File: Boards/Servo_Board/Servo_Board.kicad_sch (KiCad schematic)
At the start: 73 parts, among them J1 DB9 Microfit, J10 I2CA JST, J11 I2CB JST, J12 I2CC JST, J13 SERVO A, J14 SERVO B, J15 SERVO C, J16 SERVO D, J2 DB9 Microfit, J3 CAN1_T, J4 CAN1_T, J5 USB_B_Micro, J6 SWD JST PH, J7 UART JST, J8 AUX BATT CONN, J9 Extras JST, Q1 DMP6023LFG, U1 AZ1117C-5.0, U2 STM32G0B1RCTx, U3 TCAN1046, U4 AZ1117C-3.3, Y1 8MHz

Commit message: Somewhat done servo+adc boards
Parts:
- removed C1: 100u, Capacitor_SMD:CP_Elec_8x10.5, symbol Device:C_Polarized
- removed C2, C4: 10u, Capacitor_SMD:C_0603_1608Metric, symbol Device:C
- removed C3, C5: 22u, Capacitor_SMD:C_1206_3216Metric, symbol Device:C
- removed J1, J2: DB9 Microfit, Connector_Molex:Molex_Micro-Fit_3.0_43045-1012_2x05_P3.00mm_Vertical, symbol Connector:DE9_Socket
- removed J10: I2CA JST, Connector_JST:JST_PH_B5B-PH-K_1x05_P2.00mm_Vertical, symbol Connector_Generic:Conn_01x05
- removed J12: I2CC JST, Connector_JST:JST_PH_B5B-PH-K_1x05_P2.00mm_Vertical, symbol Connector_Generic:Conn_01x05
- removed J3, J4: CAN1_T, Connector_PinHeader_2.54mm:PinHeader_1x02_P2.54mm_Vertical, symbol Connector_Generic:Conn_01x02
- removed J5: USB_B_Micro, Connector_USB:USB_Micro-B_Amphenol_10118193-0001LF_Horizontal, symbol Connector:USB_B_Micro
- removed J6: SWD JST PH, Connector_JST:JST_PH_B4B-PH-K_1x04_P2.00mm_Vertical, symbol Connector_Generic:Conn_01x04
- removed J7: UART JST, Connector_JST:JST_PH_B3B-PH-K_1x03_P2.00mm_Vertical, symbol Connector_Generic:Conn_01x03
- removed J9: Extras JST, Connector_JST:JST_PH_B7B-PH-K_1x07_P2.00mm_Vertical, symbol Connector_Generic:Conn_01x07
- removed R11: 9K53, Resistor_SMD:R_0603_1608Metric, symbol Device:R
- removed TP14: RS422TX, TestPoint:TestPoint_Pad_1.5x1.5mm, symbol Connector:TestPoint_Small
- removed TP16: RS422RX, TestPoint:TestPoint_Pad_1.5x1.5mm, symbol Connector:TestPoint_Small
- removed TP2: ADC4S, TestPoint:TestPoint_Pad_1.5x1.5mm, symbol Connector:TestPoint_Small
- removed TP3: ADC2S, TestPoint:TestPoint_Pad_1.5x1.5mm, symbol Connector:TestPoint_Small
- removed TP31: ADC2, TestPoint:TestPoint_Pad_1.5x1.5mm, symbol Connector:TestPoint_Small
- removed TP32: ADC3, TestPoint:TestPoint_Pad_1.5x1.5mm, symbol Connector:TestPoint_Small
- removed TP4: SPISCK, TestPoint:TestPoint_Pad_1.5x1.5mm, symbol Connector:TestPoint_Small
- removed TP5: SPIMISO, TestPoint:TestPoint_Pad_1.5x1.5mm, symbol Connector:TestPoint_Small
- removed TP7: SPICS, TestPoint:TestPoint_Pad_1.5x1.5mm, symbol Connector:TestPoint_Small
- removed U1: AZ1117C-5.0, Package_TO_SOT_SMD:SOT-223-3_TabPin2, symbol Regulator_Linear:AZ1117-5.0
- added C10, C16, C19, C20: 100n, Capacitor_SMD:C_0603_1608Metric, symbol Device:C
- added C11, C13: 22u, Capacitor_SMD:C_1206_3216Metric, symbol Device:C
- added C12, C14: 10u, Capacitor_SMD:C_0603_1608Metric, symbol Device:C
- added C15, C17, C21, C22: 100u, Capacitor_SMD:CP_Elec_6.3x5.9, symbol Device:C_Polarized
- added C18: 100u, Capacitor_SMD:CP_Elec_8x10.5, symbol Device:C_Polarized
- added C23: 100n, symbol Device:C
- added D1: LED_R, LED_SMD:LED_1206_3216Metric, symbol Device:LED
- added D10: 9V 15.4VC, Diode_SMD:D_SOD-123F, symbol Device:D_TVS
- added D2: LED_G, LED_SMD:LED_1206_3216Metric, symbol Device:LED
- added D3: LED_B, LED_SMD:LED_1206_3216Metric, symbol Device:LED
- added D8: D_0.5VF, Diode_SMD:D_SOD-523, symbol Device:D_Schottky
- added D9: 2.5V Ref Zener, Package_TO_SOT_SMD:SOT-23-3, symbol Device:D_Zener
- added J1: SWD JST PH, Connector_JST:JST_PH_B4B-PH-K_1x04_P2.00mm_Vertical, symbol Connector_Generic:Conn_01x04
- added J10, J9: CAN1_T, Connector_PinHeader_2.54mm:PinHeader_1x02_P2.54mm_Vertical, symbol Connector_Generic:Conn_01x02
- added J12, J6: DB9 Microfit, Connector_Molex:Molex_Micro-Fit_3.0_43045-1012_2x05_P3.00mm_Vertical, symbol Connector:DE9_Socket
- added J2: UART JST, Connector_JST:JST_PH_B3B-PH-K_1x03_P2.00mm_Vertical, symbol Connector_Generic:Conn_01x03
- added J3: Extras JST, Connector_JST:JST_PH_B7B-PH-K_1x07_P2.00mm_Vertical, symbol Connector_Generic:Conn_01x07
- added J4: USB_B_Micro, Connector_USB:USB_Micro-B_Amphenol_10118193-0001LF_Horizontal, symbol Connector:USB_B_Micro
- added J5: I2CA JST, Connector_JST:JST_PH_B5B-PH-K_1x05_P2.00mm_Vertical, symbol Connector_Generic:Conn_01x05
- added J7: I2CB JST, Connector_JST:JST_PH_B5B-PH-K_1x05_P2.00mm_Vertical, symbol Connector_Generic:Conn_01x05
- added J8: SPI JST, Connector_JST:JST_PH_B6B-PH-K_1x06_P2.00mm_Vertical, symbol Connector_Generic:Conn_01x06
- added R10: 100K, Resistor_SMD:R_0603_1608Metric, symbol Device:R
- added R15, R16, R20, R21: 100k, Resistor_SMD:R_0603_1608Metric, symbol Device:R
- added R19: 9K53, Resistor_SMD:R_0603_1608Metric, symbol Device:R
- added R22: 22K, symbol Device:R
- added R23: 15K, symbol Device:R
- added R24: 6K2, symbol Device:R
- added R25: 4K7, symbol Device:R
- added R26: 1K5, symbol Device:R
- added R6: 0R, Resistor_SMD:R_0603_1608Metric, symbol Device:R
- added R9: 120R, Resistor_SMD:R_0603_1608Metric, symbol Device:R
- added U4: AZ1117C-5.0, Package_TO_SOT_SMD:SOT-223-3_TabPin2, symbol Regulator_Linear:AZ1117-5.0
- added U5: TPS2121RUXR, Custom:RUX0012A, symbol TS_Symbols:TPS2121RUXR
- F1: value 2A -> 5A; footprint (none) -> Fuse:Fuse_1206_3216Metric
- F2: value 2A -> 5A; footprint (none) -> Fuse:Fuse_1206_3216Metric; now fitted
- J11: value I2CB JST -> I2CC JST
- JP1, JP2: footprint (none) -> Jumper:SolderJumper-3_P1.3mm_Bridged12_RoundedPad1.0x1.5mm
- R1: value 100K -> 549R; footprint (none) -> Resistor_SMD:R_0603_1608Metric
- R11: renamed from R8; footprint (none) -> Resistor_SMD:R_0603_1608Metric
- R12: value 0R -> 100K
- R13, R14: value 0R -> 100K; now fitted; now in the parts list
- R2, R3: value 100K -> 220R; footprint (none) -> Resistor_SMD:R_0603_1608Metric
- R4: value 100K -> 0R; footprint (none) -> Resistor_SMD:R_0603_1608Metric
- R5: value 120R -> 0R; footprint (none) -> Resistor_SMD:R_0603_1608Metric; now not fitted; now left out of the parts list
- renumbered C8 to C1, C6 to C2, C7 to C3, C10 to C4, C9 to C5, C11 to C6, C12 to C7, C14 to C8, C13 to C9, D3 to D5, D2 to D6, D1 to D7, J8 to J13, J13 to J15, J15 to J16, J16 to J17, R10 to R17, R9 to R18, R6 to R7, R7 to R8, TP9 to TP1, TP8 to TP2, U2 to U1, U3 to U2, U4 to U3
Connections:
- net 2S_VOLTAGE is gone; now on net 2S+ A10: R17.2
- net USART1_RX is gone; now on net CAN2_AUX: U1.61 (PB7)
- net +3V3: now also R13.1, R14.2, R4.1, C11.1, J5.5 (Pin_5), J7.5 (Pin_5), J8.6 (Pin_6), R10.2, R23.1, R26.1; no longer R1.1, R2.1, R3.2, R4.2
- net +5V: now also R5.1, C12.1, C13.1, J5.3 (Pin_3), J7.3 (Pin_3), U4.2 (VO); no longer R13.1
- net +7V4: now also R1.1, C15.1, C17.1, C21.1, C22.1, R6.1; no longer D6.1 (K), Q1.1 (S), Q1.2 (S), Q1.3 (S), R14.1, R17.1
- net +7V4_CAN: now also J12.1, J12.5, J6.1, J6.5
- net CAN1_AUX: now also U1.64 (PC10), J6.3; no longer U1.33 (PB13)
- net CAN1_RX: now also U1.62 (PB8); no longer U1.27 (PB0)
- net CAN1_TX: now also U1.63 (PB9); no longer U1.28 (PB1)
- net CAN2_AUX: now also J12.3; no longer U1.32 (PB12)
- net CANH1: now also J12.6, J6.6, J9.1 (Pin_1)
- net CANH2: now also J12.8, J6.8, R9.2; no longer R5.2
- net CANL1: now also J10.1 (Pin_1), J12.7, J6.7
- net CANL2: now also J12.9, J6.9
- net E1: now also J3.2 (Pin_2)
- net E2: now also J3.3 (Pin_3)
- net E3: now also J3.5 (Pin_5)
- net E4: now also J3.6 (Pin_6)
- net GND: now also C10.2, C11.2, C12.2, C13.2, C14.2, C15.2, C16.2, C17.2, C18.2, C19.2, C20.2, C21.2, C22.2, D1.1 (K), D10.1 (A1), D2.1 (K), D3.1 (K), D8.1 (K), J1.2 (Pin_2), J12.2, J12.4, J2.2 (Pin_2), J3.1 (Pin_1), J3.7 (Pin_7), J4.5 (GND), J5.1 (Pin_1), J6.2, J6.4, J7.1 (Pin_1), J8.1 (Pin_1), R19.2, U4.1 (GND)
- net I2C1_SCL: now also U1.37 (PA9/UCPD1_DBCC1), J5.4 (Pin_4); no longer U1.62 (PB8)
- net I2C1_SDA: now also U1.42 (PA10/UCPD1_DBCC2), J5.2 (Pin_2); no longer U1.63 (PB9)
- net I2C2_SCL: now also J7.4 (Pin_4); no longer J11.4 (Pin_4)
- net I2C2_SDA: now also J7.2 (Pin_2); no longer J11.2 (Pin_2)
- net I2C3_SCL: now also J11.4 (Pin_4)
- net I2C3_SDA: now also J11.2 (Pin_2)
- net LED1: now also R2.1
- net NRST: now also J1.4 (Pin_4)
- net PWM_A: now also U1.38 (PC6)
- net PWM_B: now also U1.39 (PC7)
- net PWM_C: now also U1.36 (PA8)
- net PWM_D: now also U1.34 (PB14)
- net SPI_MISO: now also J8.2 (Pin_2)
- net SPI_MOSI: now also U1.24 (PA7), J8.4 (Pin_4)
- net SPI_SCK: now also J8.3 (Pin_3)
- net SWCLK: now also J1.1 (Pin_1)
- net SWDIO: now also J1.3 (Pin_3)
- net UART2_RX: now also D4.4 (K3), J2.1 (Pin_1)
- net UART2_TX: now also D4.5 (K4), J2.3 (Pin_3)
- net USB_D+: now also J4.3 (D+)
- net USB_D-: now also J4.2 (D-)
- net at D7.2 (A2), F1.1, Q1.5 (D): no longer F2.2
- net at R2.2: now also D2.2 (A); no longer U2.7 (RXD2)
- net at U2.14 (STB1): now also R10.1; no longer R4.1
- net at U2.6 (TXD2): now also R12.2; no longer R1.2
- net at U2.8 (STB2): now also R14.1; no longer R3.1
- net at J13.1 (Pin_1), J13.2 (Pin_2): now also F2.2; no longer F2.1
- net PWR_SOURCE: now reaches U1.1 (PC11)
- net PWR_SOURCE: now also R23.2, U5.9 (ST)
- net SYNC: now reaches U1.25 (PC4)
- net ~{ADC_RDY}: now reaches U1.26 (PC5)
- net 2S+ A10: now reaches U1.29 (PB2)
- net 2S+ A10: now also R19.1
- net A11: now reaches U1.30 (PB10)
- net ??PWM_AUX??: now reaches U1.35 (PB15)
- net LED2: now reaches U1.49 (PC9)
- net LED2: now also R3.1
- net at R11.1: now also J10.2 (Pin_2)
- net ADC_0 (4S) renamed POT_A A0
- net POT_A A0: now also C16.1, R16.2
- net ADC_1 (2S) renamed POT_B A1
- net POT_B A1: now also C10.1, R15.2
- net ADC_2 renamed POT_C A2
- net POT_C A2: now also C19.1, R20.2
- net ADC_3 renamed POT_D A3
- net POT_D A3: now also C20.1, R21.2
- net POT_A: no longer names the net of J15.4 (Pin_4)
- net POT_A: now also R16.1
- net POT_B: no longer names the net of J14.4 (Pin_4)
- net POT_B: now also R15.1
- net POT_C: no longer names the net of J16.4 (Pin_4)
- net POT_C: now also R20.1
- net POT_D: no longer names the net of J17.4 (Pin_4)
- net POT_D: now also R21.1
- net SPI_SD_CS renamed SPI_CS
- net SPI_CS: now also J8.5 (Pin_5)
- net USART1_TX: no longer names the net of U1.60 (PB6)
- new net: D3.2 (A), R3.2
- new net: R24.2, R25.1, U5.6 (PR1)
- new net: C23.2, D8.2 (A), D9.2 (A), R22.2, R25.2, U5.12 (GND), U5.4 (OV2), U5.5 (OV1)
- new net: D6.1 (K), Q1.1 (S), Q1.2 (S), Q1.3 (S), R24.1, U5.7 (IN1)
- new net: C14.1, C18.1, R17.1, U4.3 (VI), U5.1 (OUT), U5.8 (OUT)
- new net: D10.2 (A2), F2.1, U5.2 (IN2)
- new net: J3.4 (Pin_4), R4.2, R5.2, R6.2
- new net: R13.2, U2.7 (RXD2)
- new net: D9.1 (K), R26.2, U5.3 (CP2)
- new net: C23.1, U5.11 (SS)
- new net: R22.1, U5.10 (ILM)
- new net: D1.2 (A), R1.2
- new net: J9.2 (Pin_2), R9.1
- new net A9: U1.28 (PB1)
- new net ~{ADC_RST}: U1.27 (PB0)
- no-connect marks 17 -> 20
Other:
- note added: "1.2V dropout voltage makes V_{cr}=6.2V"
- note added: "100n gives slew limit of ~790V/s"
- note added: "Max peak: 55A Max continuous: ~6A"
- note added: "Provides RPP to stop current flowing back through TPS2121"
- note added: "RC cutoff frequency 15.9Hz"
- note added: "SPI"
- note added: "Setting to 22K gives 4.55A ILIM. ILIM=65.2/(RLIM^0.861)"
- note added: "Will switch to IN2 if PR1 drops below CP2. Want to switch at 6.3V."
- company: (none) -> Hybrid Test Stand
- title: (none) -> Servo ECU Board
- moved on the sheet: C1, C2, C3, C4, C5, C6, C7, C8, C9, D4A, D4B, D4C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

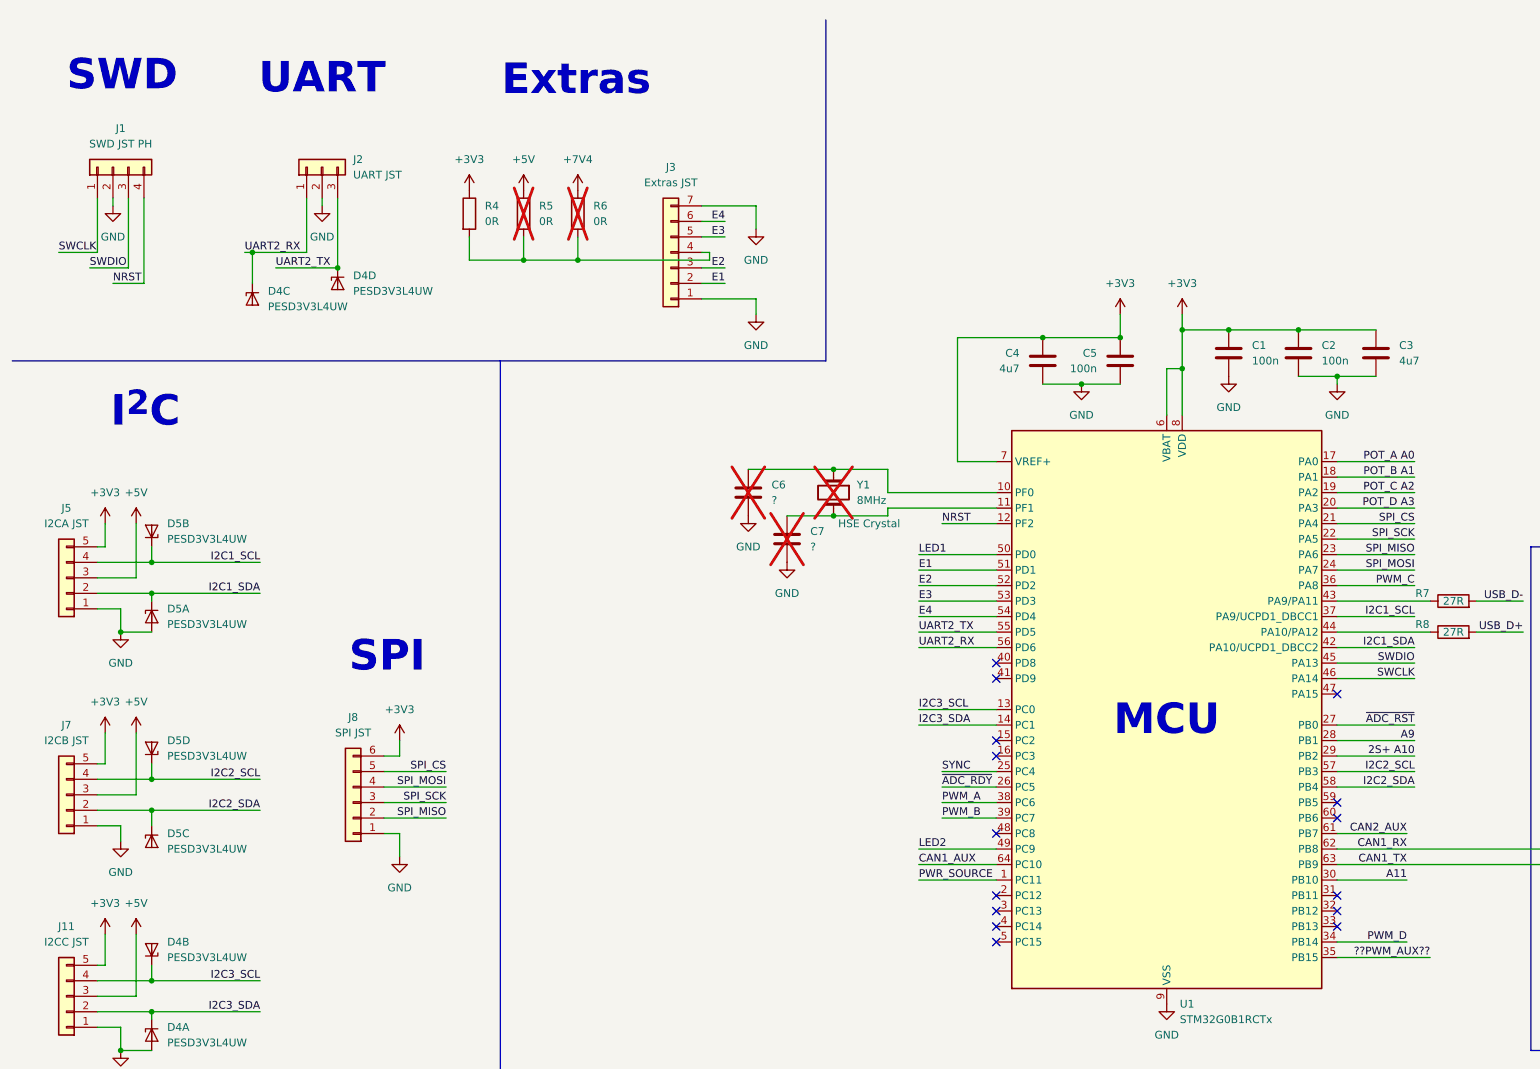
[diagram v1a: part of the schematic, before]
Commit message: Fixes and footprints
Just thermocouples todo
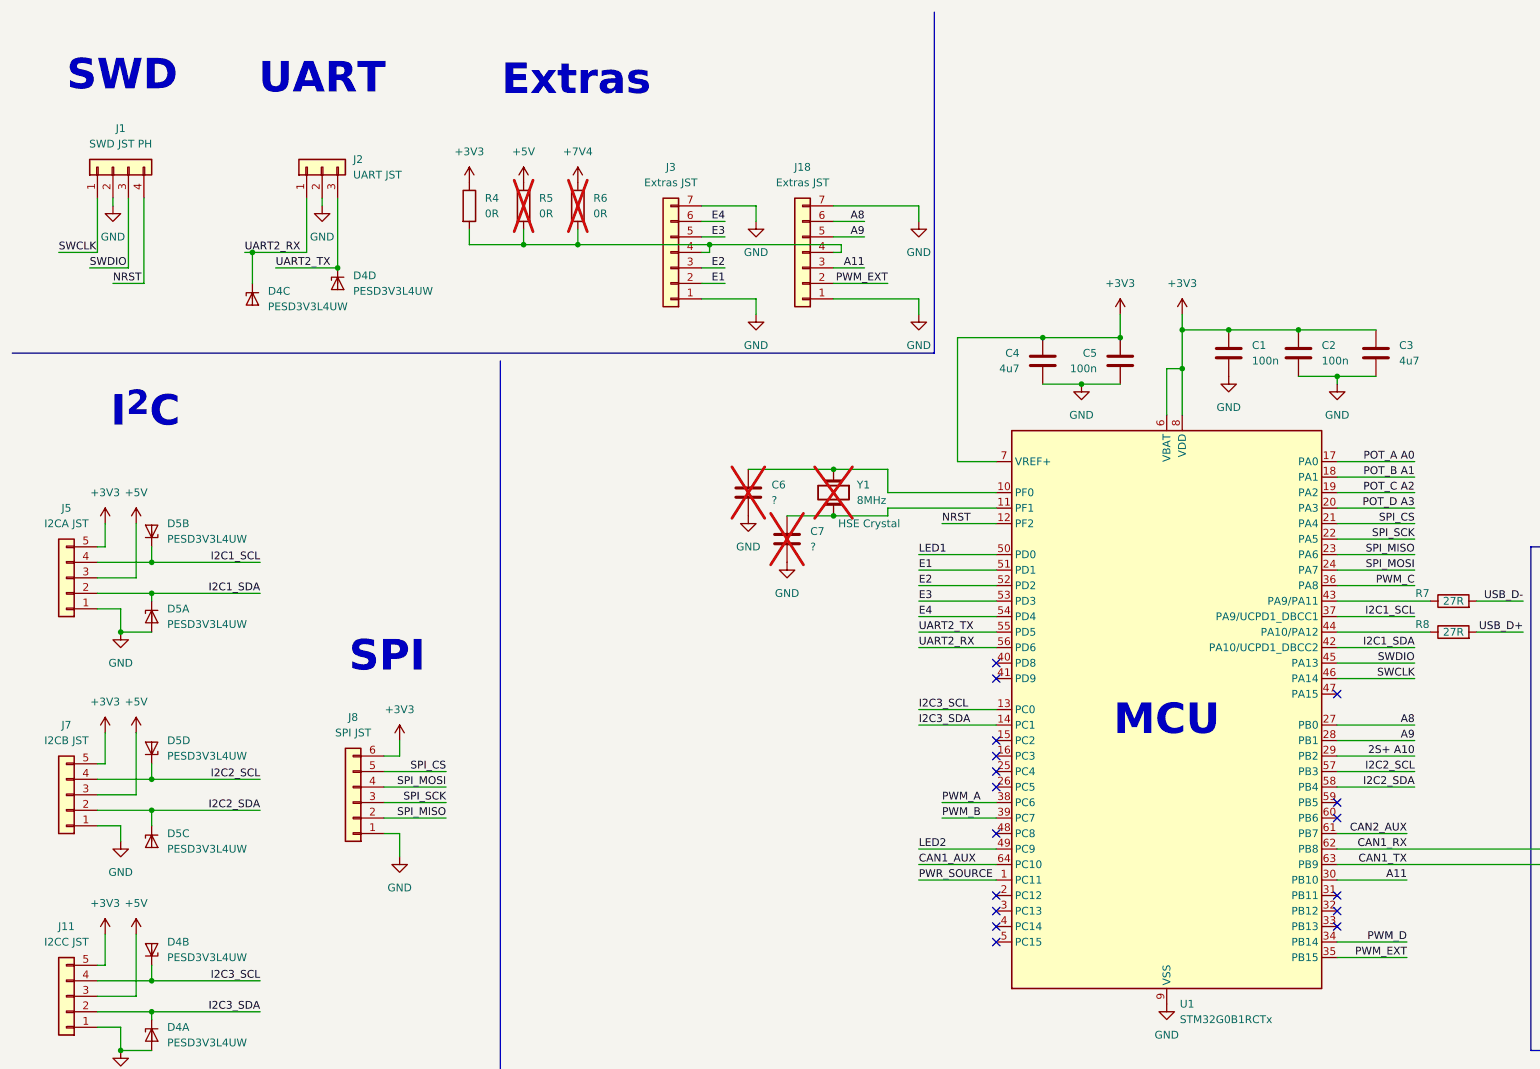
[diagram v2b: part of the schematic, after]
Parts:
- added J18: Extras JST, Connector_JST:JST_PH_B7B-PH-K_1x07_P2.00mm_Vertical, symbol Connector_Generic:Conn_01x07
- C23: footprint (none) -> Capacitor_SMD:C_0603_1608Metric
- R22, R23, R24, R25, R26: footprint (none) -> Resistor_SMD:R_0603_1608Metric
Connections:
- net A11: now also J18.3 (Pin_3)
- net A9: now also J18.5 (Pin_5)
- net GND: now also J18.1 (Pin_1), J18.7 (Pin_7)
- net at J3.4 (Pin_4), R4.2, R5.2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: now also J18.4 (Pin_4)
- net ??PWM_AUX?? renamed PWM_EXT
- net PWM_EXT: now also J18.2 (Pin_2)
- net SYNC: no longer names the net of U1.25 (PC4)
- net ~{ADC_RDY}: no longer names the net of U1.26 (PC5)
- net ~{ADC_RST} renamed A8
- net A8: now also J18.6 (Pin_6)
- no-connect marks 20 -> 22
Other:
- moved on the sheet: R4, R5, R6

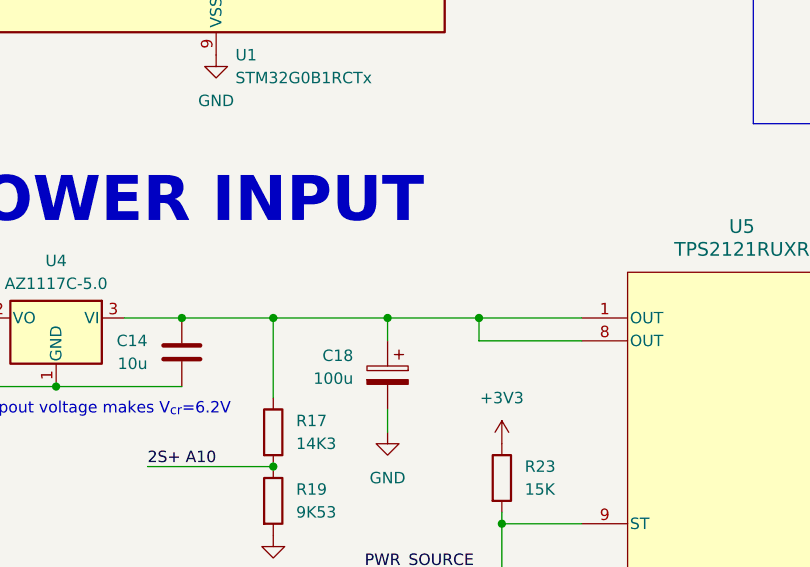
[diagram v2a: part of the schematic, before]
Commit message: Added switch to servo board
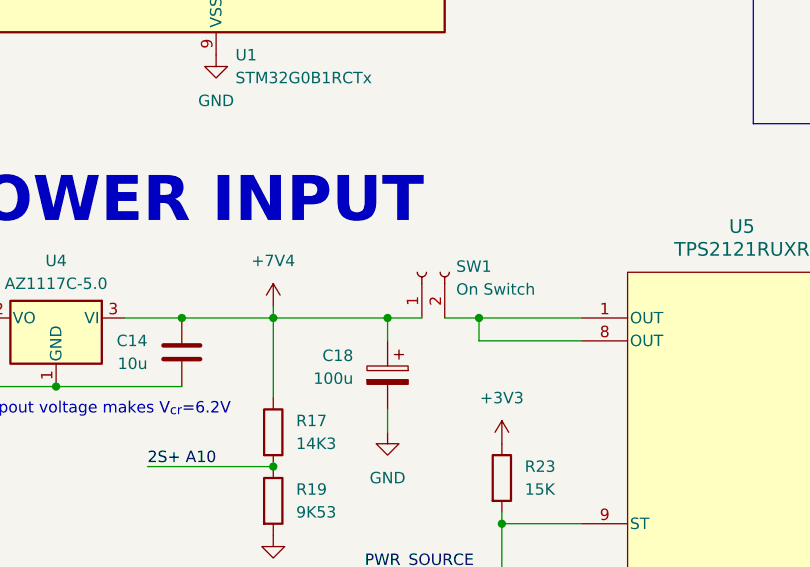
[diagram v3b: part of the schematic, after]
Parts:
- added SW1: On Switch, Connector_Molex:Molex_Micro-Fit_3.0_43650-0215_1x02_P3.00mm_Vertical, symbol Connector:Conn_01x02_Socket
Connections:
- net +7V4: now also C14.1, C18.1, R17.1, U4.3 (VI), SW1.1 (Pin_1)
- new net: SW1.2 (Pin_2), U5.1 (OUT), U5.8 (OUT)
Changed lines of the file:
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@@
 	(wire
 		(pts
+			(xy 208.28 201.93) (xy 208.28 203.2)
+		)
+		(stroke
+			(width 0)
+			(type default)
+		)
+	)
+	(wire
+		(pts
 			(xy 386.08 80.01) (xy 394.97 80.01)
 		)
@@
 	(wire
 		(pts
+			(xy 227.33 203.2) (xy 231.14 203.2)
+		)
+		(stroke
+			(width 0)
+			(type default)
+		)
+	)
+	(wire
+		(pts
 			(xy 229.87 90.17) (xy 242.57 90.17)
 		)
@@
 	(wire
 		(pts
-			(xy 220.98 203.2) (xy 231.14 203.2)
+			(xy 220.98 203.2) (xy 224.79 203.2)
 		)
 		(stroke
@@
 	)
 	(symbol
+		(lib_id "power:+3V3")
+		(at 208.28 201.93 0)
+		(mirror y)
+		(unit 1)
+		(exclude_from_sim no)
+		(in_bom yes)
+		(on_board yes)
+		(dnp no)
+		(fields_autoplaced yes)
+		(property "Reference" "#PWR067"
+			(at 208.28 205.74 0)
+			(effects
+				(font
+					(size 1.27 1.27)
+				)
+				(hide yes)
+			)
+		)
+		(property "Value" "+7V4"
+			(at 208.28 196.85 0)
+			(effects
+				(font
+					(size 1.27 1.27)
+				)
+			)
+		)
+		(property "Footprint" ""
+			(at 208.28 201.93 0)
+			(effects
+				(font
+					(size 1.27 1.27)
+				)
+				(hide yes)
+			)
+		)
+		(property "Datasheet" ""
+			(at 208.28 201.93 0)
+			(effects
+				(font
+					(size 1.27 1.27)
+				)
+				(hide yes)
+			)
+		)
+		(property "Description" "Power symbol creates a global label with name \"+7V4\""
+			(at 208.28 201.93 0)
+			(effects
+				(font
+					(size 1.27 1.27)
+				)
+				(hide yes)
+			)
+		)
+		(pin "1"
+		)
+		(instances
+			(project "Servo_Board"
+				(path "/2ef6413b-3d6c-4280-a117-e3d1b74ccf03"
+					(reference "#PWR067")
+					(unit 1)
+				)
+			)
+		)
+	)
+	(symbol
 		(lib_id "Device:R")
 		(at 105.41 43.18 0)
@@
 					(unit 1)
 				)
+			)
+		)
+	)
+	(symbol
+		(lib_id "Connector:Conn_01x02_Socket")
+		(at 224.79 198.12 90)
+		(unit 1)
+		(exclude_from_sim no)
+		(in_bom yes)
+		(on_board yes)
+		(dnp no)
+		(fields_autoplaced yes)
+		(property "Reference" "SW1"
+			(at 228.6 197.4849 90)
+			(effects
+				(font
+					(size 1.27 1.27)
+				)
+				(justify right)
+			)
+		)
+		(property "Value" "On Switch"
+			(at 228.6 200.0249 90)
+			(effects
+				(font
+					(size 1.27 1.27)
+				)
+				(justify right)
+			)
+		)
+		(property "Footprint" "Connector_Molex:Molex_Micro-Fit_3.0_43650-0215_1x02_P3.00mm_Vertical"
+			(at 224.79 198.12 0)
+			(effects
+				(font
+					(size 1.27 1.27)
+				)
+				(hide yes)
+			)
+		)
+		(property "Datasheet" "https://tools.molex.com/pdm_docs/ps/PS-43650.pdf"
+			(at 224.79 198.12 0)
+			(effects
+				(font
+					(size 1.27 1.27)
+				)
+				(hide yes)
+			)
+		)
+		(property "Description" "Generic connector, single row, 01x02, script generated"
+			(at 224.79 198.12 0)
+			(effects
+				(font
+					(size 1.27 1.27)
+				)
+				(hide yes)
+			)
+		)
+		(property "MPN" "436500228"
+			(at 224.79 198.12 90)
+			(effects
+				(font
+					(size 1.27 1.27)
+				)
+				(hide yes)
+			)
+		)
+		(property "Sim.Type" ""
+			(at 224.79 198.12 0)
+			(effects
+				(font
+					(size 1.27 1.27)
+				)
+			)
+		)
+		(pin "2"
+		)
+		(pin "1"
+		)
+		(instances
+			(project "Servo_Board"
+				(path "/2ef6413b-3d6c-4280-a117-e3d1b74ccf03"
+					(reference "SW1")
+					(unit 1)
+				)

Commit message: Servo nearing completion and ADC 50% layed out
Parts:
- removed C18: 100u, Capacitor_SMD:CP_Elec_8x10.5, symbol Device:C_Polarized
- removed J13: AUX BATT CONN, Connector_JST:JST_PH_B4B-PH-K_1x04_P2.00mm_Vertical, symbol Connector_Generic:Conn_01x04
- added J19: Backup Power, Connector_Molex:Molex_Micro-Fit_3.0_43650-0315_1x03_P3.00mm_Vertical, symbol Connector_Generic:Conn_01x03
- added R27: R, Resistor_SMD:R_0603_1608Metric, symbol Device:R
- added R28, R29, R30: 10K, Resistor_SMD:R_0603_1608Metric, symbol Device:R
- J10: value CAN1_T -> CAN2_T
- J12, J6: footprint Connector_Molex:Molex_Micro-Fit_3.0_43045-1012_2x05_P3.00mm_Vertical -> Connector_Dsub:DSUB-9_Pins_Horizontal_P2.77x2.84mm_EdgePinOffset7.70mm_Housed_MountingHolesOffset9.12mm
- R4: value 0R -> 10K
- R5, R6: value 0R -> 10K; now fitted; now in the parts list
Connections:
- net +3V3: now also J18.4 (Pin_4), J3.4 (Pin_4), R5.1, R6.1, R27.2, R28.1, R29.1, R30.1
- net +5V: no longer J11.3 (Pin_3), J5.3 (Pin_3), J7.3 (Pin_3), R5.1
- net +7V4: no longer R6.1
- net CANH2: now also R11.2; no longer R9.2
- net CANL1: now also R9.2; no longer J10.1 (Pin_1)
- net CANL2: now also J10.1 (Pin_1); no longer R11.2
- net GND: now also J19.2 (Pin_2), J19.3 (Pin_3)
- net I2C1_SCL: now also R29.2
- net I2C1_SDA: now also R30.2
- net I2C2_SCL: now also D4.3 (K2), R6.2; no longer D5.5 (K4)
- net I2C2_SDA: now also D4.1 (K1), R28.2; no longer D5.4 (K3)
- net I2C3_SCL: now also D5.5 (K4), R4.2; no longer D4.3 (K2)
- net I2C3_SDA: now also D5.4 (K3), R5.2; no longer D4.1 (K1)
- net NRST: now also R27.1
- net SPI_MISO: now also J8.3 (Pin_3); no longer J8.2 (Pin_2)
- net SPI_MOSI: now also J8.2 (Pin_2); no longer J8.4 (Pin_4)
- net SPI_SCK: now also J8.4 (Pin_4); no longer J8.3 (Pin_3)
- net at F2.2: now also J19.1 (Pin_1)
- no-connect marks 22 -> 25
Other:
- moved on the sheet: D4A, D4B, D5C, D5D, J10, J8, R11, R9

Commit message: Completed with manufacturing files
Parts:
- added TP16: 7.4V, TestPoint:TestPoint_Pad_D1.0mm, symbol Connector:TestPoint
- added TP17: 5V, TestPoint:TestPoint_Pad_D1.0mm, symbol Connector:TestPoint
- added TP18: 3.3V, TestPoint:TestPoint_Pad_D1.0mm, symbol Connector:TestPoint
- added TP19, TP20: GND, TestPoint:TestPoint_Bridge_Pitch2.54mm_Drill1.3mm, symbol Connector:TestPoint
- added TP3: 2S+, TestPoint:TestPoint_Pad_D1.0mm, symbol Connector:TestPoint_Small
- added TP4: P_SOURCE, TestPoint:TestPoint_Pad_D1.0mm, symbol Connector:TestPoint_Small
- D1: value LED_R -> LED_B
- D3: value LED_B -> LED_R
- TP1, TP2: footprint TestPoint:TestPoint_Pad_1.5x1.5mm -> TestPoint:TestPoint_Pad_D1.0mm
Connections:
- net +3V3: now also TP18.1
- net +5V: now also TP17.1
- net +7V4: now also TP16.1
- net 2S+ A10: now also TP3.1
- net GND: now also TP19.1, TP20.1
- net PWR_SOURCE: now also TP4.1

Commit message: Cleaning out code for firmware
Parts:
- J12: MPN 0430451027 -> A-DF 09 A/KG-T2S
- J6: MPN 0430451027 -> A-DS 09 A/KG-T2S
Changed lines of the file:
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@@
 			)
 		)
-		(property "MPN" "0430451027"
+		(property "MPN" "A-DS 09 A/KG-T2S"
 			(at 372.11 111.76 0)
 			(effects
@@
 			)
 		)
-		(property "MPN" "0430451027"
+		(property "MPN" "A-DF 09 A/KG-T2S"
 			(at 372.11 189.23 0)
 			(effects
